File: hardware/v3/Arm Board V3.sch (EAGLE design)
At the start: 66 parts, among them CN1 1X4-BIG, IC1 L6208D, IC2 L6208D, IC3 L6208D, IC4 7812TV, IC5 7812TV, Q3 Q_LTC490, U1 MAX3468CPA, U2 XBEE-1B3

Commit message: 3V3 Vreg
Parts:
- added C18, C19: 0.1uF, SparkFun-Capacitors:0.1UF-25V(+80/-20%)(0603)
- added R17: 240, SparkFun-Resistors:RESISTOR0805-RES
- added R18: 390, SparkFun-Resistors:RESISTOR0805-RES
- added U3: V_REG_317SMD, SparkFun-PowerIC:V_REG_317SMD
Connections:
- new net N$12: R17.1, R18.2, U3.ADJ
- net +3V3: now also C19.1, R17.2, U3.OUT
- net GND: now also C18.2, C19.2, R18.1
- net VIN: now also C18.1, U3.IN
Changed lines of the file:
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@@
 <part name="C15" library="SparkFun-Capacitors" deviceset="0.1UF-25V(+80/-20%)(0603)" device="" value="0.1uF"/>
 <part name="C17" library="SparkFun-Capacitors" deviceset="0.1UF-25V(+80/-20%)(0603)" device="" value="0.1uF"/>
+<part name="U3" library="SparkFun-PowerIC" deviceset="V_REG_317" device="SMD"/>
+<part name="GND20" library="SparkFun-Aesthetics" deviceset="GND" device=""/>
+<part name="R17" library="SparkFun-Resistors" deviceset="RESISTOR" device="0805-RES" value="240"/>
+<part name="R18" library="SparkFun-Resistors" deviceset="RESISTOR" device="0805-RES" value="390"/>
+<part name="C18" library="SparkFun-Capacitors" deviceset="0.1UF-25V(+80/-20%)(0603)" device="" value="0.1uF"/>
+<part name="C19" library="SparkFun-Capacitors" deviceset="0.1UF-25V(+80/-20%)(0603)" device="" value="0.1uF"/>
 </parts>
 <sheets>
@@
 <instance part="C15" gate="G$1" x="104.14" y="33.02"/>
 <instance part="C17" gate="G$1" x="109.22" y="33.02"/>
+<instance part="U3" gate="G$1" x="101.6" y="7.62"/>
+<instance part="GND20" gate="1" x="101.6" y="-20.32"/>
+<instance part="R17" gate="G$1" x="109.22" y="-5.08"/>
+<instance part="R18" gate="G$1" x="101.6" y="-10.16" rot="R90"/>
+<instance part="C18" gate="G$1" x="86.36" y="2.54"/>
+<instance part="C19" gate="G$1" x="116.84" y="2.54"/>
 </instances>
 <busses>
@@
 <pinref part="C17" gate="G$1" pin="2"/>
 </segment>
+<segment>
+<pinref part="GND20" gate="1" pin="GND"/>
+<pinref part="R18" gate="G$1" pin="1"/>
+<wire x1="101.6" y1="-15.24" x2="101.6" y2="-17.78" width="0.1524" layer="91"/>
+<pinref part="C19" gate="G$1" pin="2"/>
+<wire x1="116.84" y1="0" x2="116.84" y2="-17.78" width="0.1524" layer="91"/>
+<wire x1="116.84" y1="-17.78" x2="101.6" y2="-17.78" width="0.1524" layer="91"/>
+<pinref part="C18" gate="G$1" pin="2"/>
+<wire x1="101.6" y1="-17.78" x2="86.36" y2="-17.78" width="0.1524" layer="91"/>
+<wire x1="86.36" y1="-17.78" x2="86.36" y2="0" width="0.1524" layer="91"/>
+<junction x="101.6" y="-17.78"/>
+</segment>
 </net>
 <net name="A1_1" class="0">
@@
 <pinref part="C17" gate="G$1" pin="1"/>
 </segment>
+<segment>
+<pinref part="U3" gate="G$1" pin="IN"/>
+<pinref part="C18" gate="G$1" pin="1"/>
+<wire x1="86.36" y1="7.62" x2="93.98" y2="7.62" width="0.1524" layer="91"/>
+<wire x1="86.36" y1="7.62" x2="81.28" y2="7.62" width="0.1524" layer="91"/>
+<label x="81.28" y="7.62" size="1.778" layer="95"/>
+</segment>
 </net>
 <net name="A1_3" class="0">
@@
 </segment>
 </net>
+<net name="N$12" class="0">
+<segment>
+<pinref part="U3" gate="G$1" pin="ADJ"/>
+<pinref part="R18" gate="G$1" pin="2"/>
+<wire x1="101.6" y1="-5.08" x2="101.6" y2="0" width="0.1524" layer="91"/>
+<pinref part="R17" gate="G$1" pin="1"/>
+<wire x1="104.14" y1="-5.08" x2="101.6" y2="-5.08" width="0.1524" layer="91"/>
+<junction x="101.6" y="-5.08"/>
+</segment>
+</net>
+<net name="+3V3" class="0">
+<segment>
+<pinref part="U3" gate="G$1" pin="OUT"/>
+<pinref part="C19" gate="G$1" pin="1"/>
+<wire x1="116.84" y1="7.62" x2="114.3" y2="7.62" width="0.1524" layer="91"/>
+<pinref part="R17" gate="G$1" pin="2"/>
+<wire x1="114.3" y1="7.62" x2="109.22" y2="7.62" width="0.1524" layer="91"/>
+<wire x1="114.3" y1="-5.08" x2="114.3" y2="7.62" width="0.1524" layer="91"/>
+<junction x="114.3" y="7.62"/>
+<wire x1="116.84" y1="7.62" x2="121.92" y2="7.62" width="0.1524" layer="91"/>
+<label x="116.84" y="7.62" size="1.778" layer="95"/>
+</segment>
+</net>

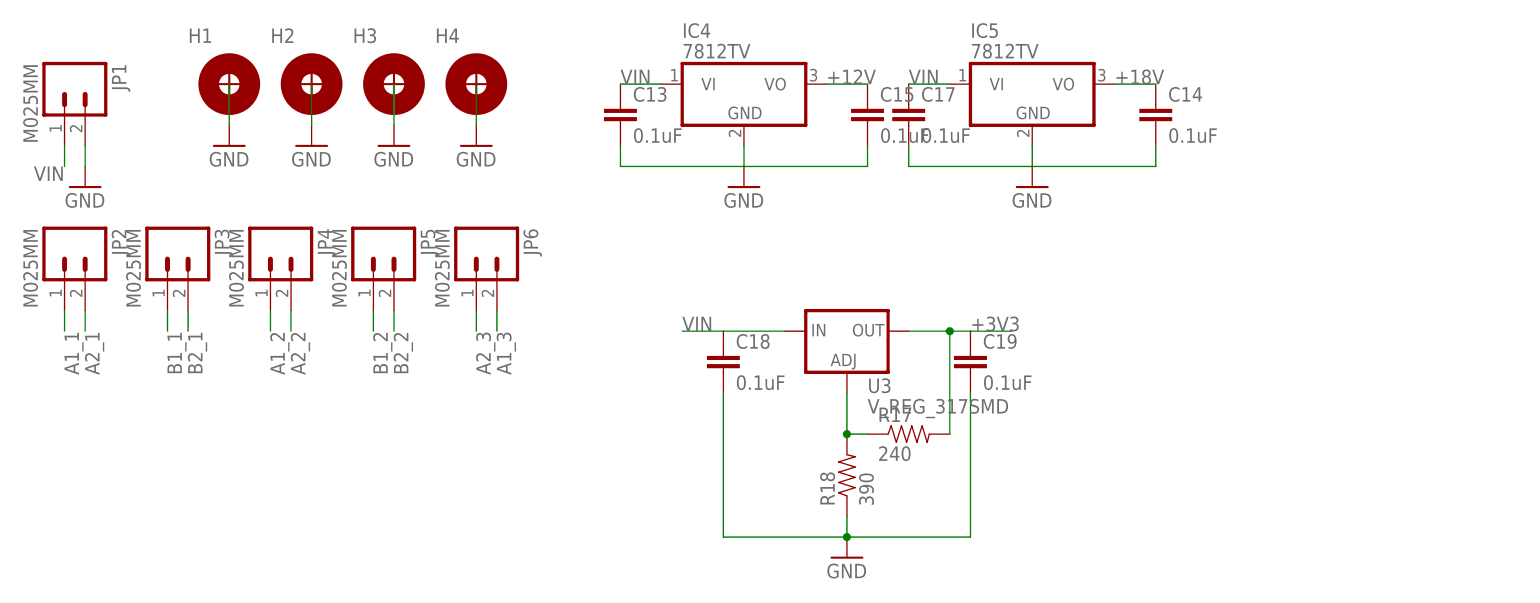
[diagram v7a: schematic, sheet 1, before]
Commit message: 5v and 3v3 power rails
Added a second 12v regulator to drive the 5v and 3v3 regulator
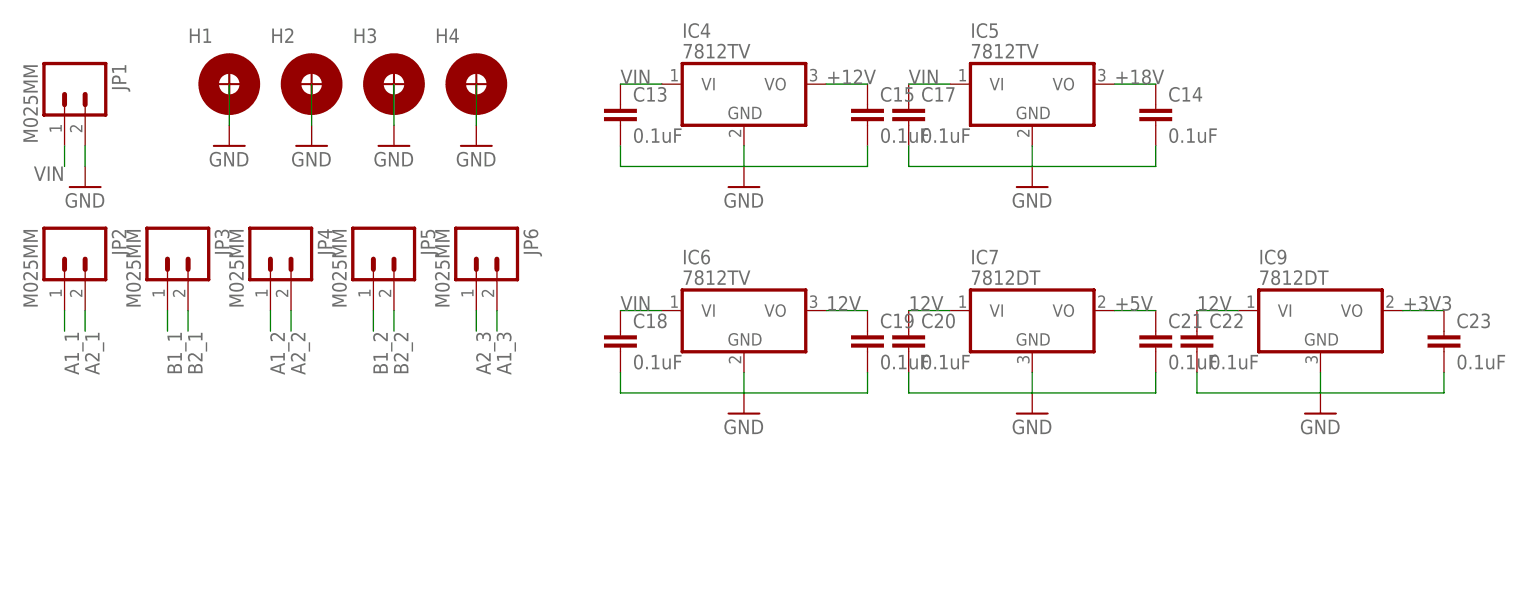
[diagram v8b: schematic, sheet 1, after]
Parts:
- removed R17: 240, SparkFun-Resistors:RESISTOR0805-RES
- removed R18: 390, SparkFun-Resistors:RESISTOR0805-RES
- removed U3: V_REG_317SMD, SparkFun-PowerIC:V_REG_317SMD
- added C20, C21, C22, C23: 0.1uF, SparkFun-Capacitors:0.1UF-25V(+80/-20%)(0603)
- added IC6: 7812TV, linear:7812TV
- added IC7, IC9: 7812DT, linear:7812DT
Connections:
- removed net N$12: R17.1, R18.2, U3.ADJ
- new net 12V: C19.1, C20.1, C22.1, IC6.VO, IC7.VI, IC9.VI
- net +3V3: now also C23.1, IC9.VO; no longer C19.1, R17.2, U3.OUT
- net +5V: now also C21.1, IC7.VO
- net GND: now also C20.2, C21.2, C22.2, C23.2, IC6.GND, IC7.GND, IC9.GND; no longer R18.1
- net VIN: now also IC6.VI; no longer U3.IN
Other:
- moved on the sheet: C18, C19
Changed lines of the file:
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@@
 <part name="C15" library="SparkFun-Capacitors" deviceset="0.1UF-25V(+80/-20%)(0603)" device="" value="0.1uF"/>
 <part name="C17" library="SparkFun-Capacitors" deviceset="0.1UF-25V(+80/-20%)(0603)" device="" value="0.1uF"/>
-<part name="U3" library="SparkFun-PowerIC" deviceset="V_REG_317" device="SMD"/>
 <part name="GND20" library="SparkFun-Aesthetics" deviceset="GND" device=""/>
-<part name="R17" library="SparkFun-Resistors" deviceset="RESISTOR" device="0805-RES" value="240"/>
-<part name="R18" library="SparkFun-Resistors" deviceset="RESISTOR" device="0805-RES" value="390"/>
 <part name="C18" library="SparkFun-Capacitors" deviceset="0.1UF-25V(+80/-20%)(0603)" device="" value="0.1uF"/>
 <part name="C19" library="SparkFun-Capacitors" deviceset="0.1UF-25V(+80/-20%)(0603)" device="" value="0.1uF"/>
+<part name="IC6" library="linear" deviceset="78*" device="TV" technology="12" value="7812TV"/>
+<part name="GND23" library="SparkFun-Aesthetics" deviceset="GND" device=""/>
+<part name="C20" library="SparkFun-Capacitors" deviceset="0.1UF-25V(+80/-20%)(0603)" device="" value="0.1uF"/>
+<part name="C21" library="SparkFun-Capacitors" deviceset="0.1UF-25V(+80/-20%)(0603)" device="" value="0.1uF"/>
+<part name="IC7" library="linear" deviceset="78*" device="DT" technology="12" value="7812DT"/>
+<part name="GND24" library="SparkFun-Aesthetics" deviceset="GND" device=""/>
+<part name="C22" library="SparkFun-Capacitors" deviceset="0.1UF-25V(+80/-20%)(0603)" device="" value="0.1uF"/>
+<part name="C23" library="SparkFun-Capacitors" deviceset="0.1UF-25V(+80/-20%)(0603)" device="" value="0.1uF"/>
+<part name="IC9" library="linear" deviceset="78*" device="DT" technology="12" value="7812DT"/>
 </parts>
 <sheets>
@@
 <instance part="C15" gate="G$1" x="104.14" y="33.02"/>
 <instance part="C17" gate="G$1" x="109.22" y="33.02"/>
-<instance part="U3" gate="G$1" x="101.6" y="7.62"/>
-<instance part="GND20" gate="1" x="101.6" y="-20.32"/>
-<instance part="R17" gate="G$1" x="109.22" y="-5.08"/>
-<instance part="R18" gate="G$1" x="101.6" y="-10.16" rot="R90"/>
-<instance part="C18" gate="G$1" x="86.36" y="2.54"/>
-<instance part="C19" gate="G$1" x="116.84" y="2.54"/>
+<instance part="GND20" gate="1" x="88.9" y="-2.54"/>
+<instance part="C18" gate="G$1" x="73.66" y="5.08"/>
+<instance part="C19" gate="G$1" x="104.14" y="5.08"/>
+<instance part="IC6" gate="A1" x="88.9" y="10.16"/>
+<instance part="GND23" gate="1" x="124.46" y="-2.54"/>
+<instance part="C20" gate="G$1" x="109.22" y="5.08"/>
+<instance part="C21" gate="G$1" x="139.7" y="5.08"/>
+<instance part="IC7" gate="A1" x="124.46" y="10.16"/>
+<instance part="GND24" gate="1" x="160.02" y="-2.54"/>
+<instance part="C22" gate="G$1" x="144.78" y="5.08"/>
+<instance part="C23" gate="G$1" x="175.26" y="5.08"/>
+<instance part="IC9" gate="A1" x="160.02" y="10.16"/>
 </instances>
 <busses>
@@
 </segment>
 <segment>
+<wire x1="88.9" y1="2.54" x2="88.9" y2="0" width="0.1524" layer="91"/>
 <pinref part="GND20" gate="1" pin="GND"/>
-<pinref part="R18" gate="G$1" pin="1"/>
-<wire x1="101.6" y1="-15.24" x2="101.6" y2="-17.78" width="0.1524" layer="91"/>
+<wire x1="88.9" y1="0" x2="73.66" y2="0" width="0.1524" layer="91"/>
+<wire x1="73.66" y1="0" x2="73.66" y2="2.54" width="0.1524" layer="91"/>
+<wire x1="88.9" y1="0" x2="104.14" y2="0" width="0.1524" layer="91"/>
+<wire x1="104.14" y1="0" x2="104.14" y2="2.54" width="0.1524" layer="91"/>
+<pinref part="C18" gate="G$1" pin="2"/>
 <pinref part="C19" gate="G$1" pin="2"/>
-<wire x1="116.84" y1="0" x2="116.84" y2="-17.78" width="0.1524" layer="91"/>
-<wire x1="116.84" y1="-17.78" x2="101.6" y2="-17.78" width="0.1524" layer="91"/>
-<pinref part="C18" gate="G$1" pin="2"/>
-<wire x1="101.6" y1="-17.78" x2="86.36" y2="-17.78" width="0.1524" layer="91"/>
-<wire x1="86.36" y1="-17.78" x2="86.36" y2="0" width="0.1524" layer="91"/>
-<junction x="101.6" y="-17.78"/>
+<pinref part="IC6" gate="A1" pin="GND"/>
+</segment>
+<segment>
+<wire x1="124.46" y1="2.54" x2="124.46" y2="0" width="0.1524" layer="91"/>
+<pinref part="GND23" gate="1" pin="GND"/>
+<wire x1="124.46" y1="0" x2="109.22" y2="0" width="0.1524" layer="91"/>
+<wire x1="109.22" y1="0" x2="109.22" y2="2.54" width="0.1524" layer="91"/>
+<wire x1="124.46" y1="0" x2="139.7" y2="0" width="0.1524" layer="91"/>
+<wire x1="139.7" y1="0" x2="139.7" y2="2.54" width="0.1524" layer="91"/>
+<pinref part="C20" gate="G$1" pin="2"/>
+<pinref part="C21" gate="G$1" pin="2"/>
+<pinref part="IC7" gate="A1" pin="GND"/>
+</segment>
+<segment>
+<wire x1="160.02" y1="2.54" x2="160.02" y2="0" width="0.1524" layer="91"/>
+<pinref part="GND24" gate="1" pin="GND"/>
+<wire x1="160.02" y1="0" x2="144.78" y2="0" width="0.1524" layer="91"/>
+<wire x1="144.78" y1="0" x2="144.78" y2="2.54" width="0.1524" layer="91"/>
+<wire x1="160.02" y1="0" x2="175.26" y2="0" width="0.1524" layer="91"/>
+<wire x1="175.26" y1="0" x2="175.26" y2="2.54" width="0.1524" layer="91"/>
+<pinref part="C22" gate="G$1" pin="2"/>
+<pinref part="C23" gate="G$1" pin="2"/>
+<pinref part="IC9" gate="A1" pin="GND"/>
 </segment>
 </net>
@@
 </segment>
 <segment>
-<pinref part="U3" gate="G$1" pin="IN"/>
+<wire x1="78.74" y1="10.16" x2="73.66" y2="10.16" width="0.1524" layer="91"/>
+<label x="73.66" y="10.16" size="1.778" layer="95"/>
 <pinref part="C18" gate="G$1" pin="1"/>
-<wire x1="86.36" y1="7.62" x2="93.98" y2="7.62" width="0.1524" layer="91"/>
-<wire x1="86.36" y1="7.62" x2="81.28" y2="7.62" width="0.1524" layer="91"/>
-<label x="81.28" y="7.62" size="1.778" layer="95"/>
+<pinref part="IC6" gate="A1" pin="VI"/>
 </segment>
 </net>
@@
 </segment>
 </net>
-<net name="N$12" class="0">
-<segment>
-<pinref part="U3" gate="G$1" pin="ADJ"/>
-<pinref part="R18" gate="G$1" pin="2"/>
-<wire x1="101.6" y1="-5.08" x2="101.6" y2="0" width="0.1524" layer="91"/>
-<pinref part="R17" gate="G$1" pin="1"/>
-<wire x1="104.14" y1="-5.08" x2="101.6" y2="-5.08" width="0.1524" layer="91"/>
-<junction x="101.6" y="-5.08"/>
+<net name="12V" class="0">
+<segment>
+<wire x1="99.06" y1="10.16" x2="104.14" y2="10.16" width="0.1524" layer="91"/>
+<label x="99.06" y="10.16" size="1.778" layer="95"/>
+<pinref part="C19" gate="G$1" pin="1"/>
+<pinref part="IC6" gate="A1" pin="VO"/>
+</segment>
+<segment>
+<wire x1="114.3" y1="10.16" x2="109.22" y2="10.16" width="0.1524" layer="91"/>
+<label x="109.22" y="10.16" size="1.778" layer="95"/>
+<pinref part="C20" gate="G$1" pin="1"/>
+<pinref part="IC7" gate="A1" pin="VI"/>
+</segment>
+<segment>
+<wire x1="149.86" y1="10.16" x2="144.78" y2="10.16" width="0.1524" layer="91"/>
+<label x="144.78" y="10.16" size="1.778" layer="95"/>
+<pinref part="C22" gate="G$1" pin="1"/>
+<pinref part="IC9" gate="A1" pin="VI"/>
+</segment>
+</net>
+<net name="+5V" class="0">
+<segment>
+<wire x1="134.62" y1="10.16" x2="139.7" y2="10.16" width="0.1524" layer="91"/>
+<label x="134.62" y="10.16" size="1.778" layer="95"/>
+<pinref part="C21" gate="G$1" pin="1"/>
+<pinref part="IC7" gate="A1" pin="VO"/>
 </segment>
 </net>
 <net name="+3V3" class="0">
 <segment>
-<pinref part="U3" gate="G$1" pin="OUT"/>
-<pinref part="C19" gate="G$1" pin="1"/>
-<wire x1="116.84" y1="7.62" x2="114.3" y2="7.62" width="0.1524" layer="91"/>
-<pinref part="R17" gate="G$1" pin="2"/>
-<wire x1="114.3" y1="7.62" x2="109.22" y2="7.62" width="0.1524" layer="91"/>
-<wire x1="114.3" y1="-5.08" x2="114.3" y2="7.62" width="0.1524" layer="91"/>
-<junction x="114.3" y="7.62"/>
-<wire x1="116.84" y1="7.62" x2="121.92" y2="7.62" width="0.1524" layer="91"/>
-<label x="116.84" y="7.62" size="1.778" layer="95"/>
-</segment>
-</net>
+<wire x1="170.18" y1="10.16" x2="175.26" y2="10.16" width="0.1524" layer="91"/>
+<label x="170.18" y="10.16" size="1.778" layer="95"/>
+<pinref part="C23" gate="G$1" pin="1"/>
+<pinref part="IC9" gate="A1" pin="VO"/>
+</segment>
+</net>
